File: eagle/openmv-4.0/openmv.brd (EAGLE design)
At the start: 25.4 x 33.3 mm, 42 parts, among them U1 OV9650, U2 USD-47571, U3 ADP322, U4 STM32F407LQFP100, U5 BEAD, X1 USB-MICROB, Y2 RESONATORSMD

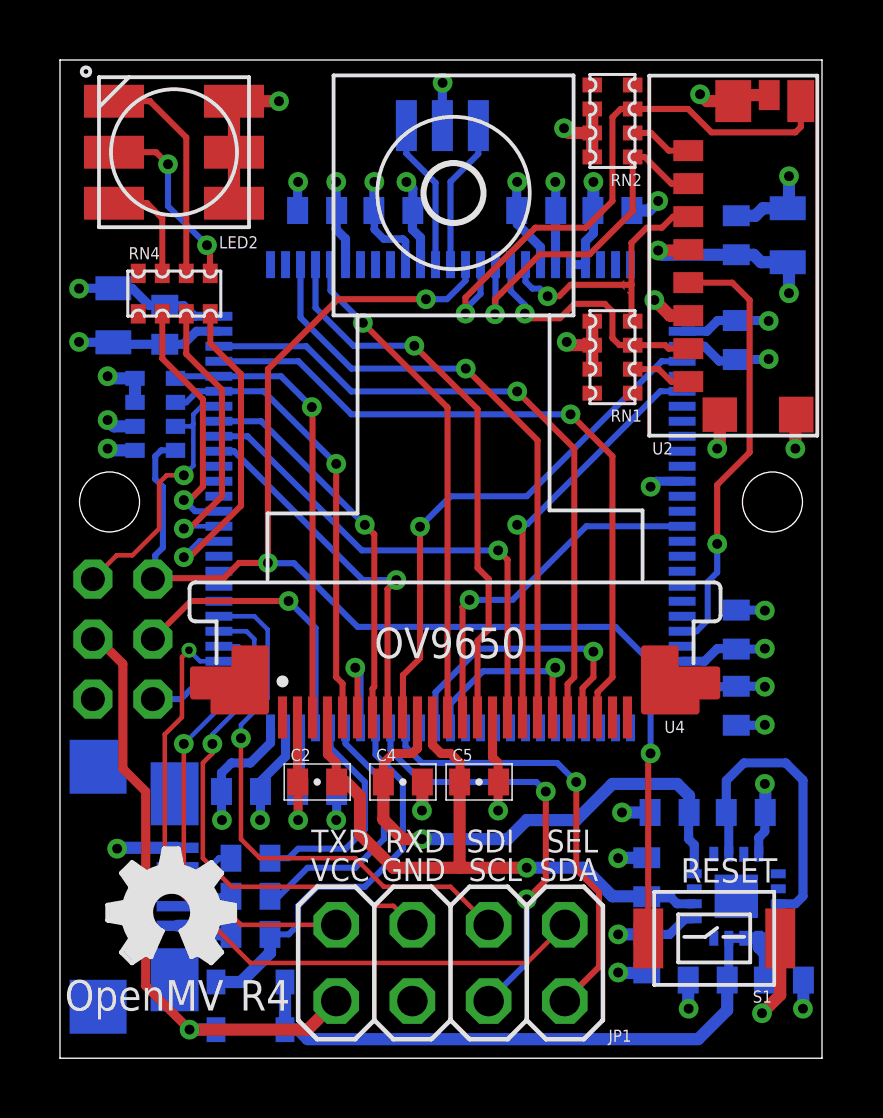
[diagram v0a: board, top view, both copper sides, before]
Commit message: Update REV4
* Add regulator test points
* Remove 10mil via
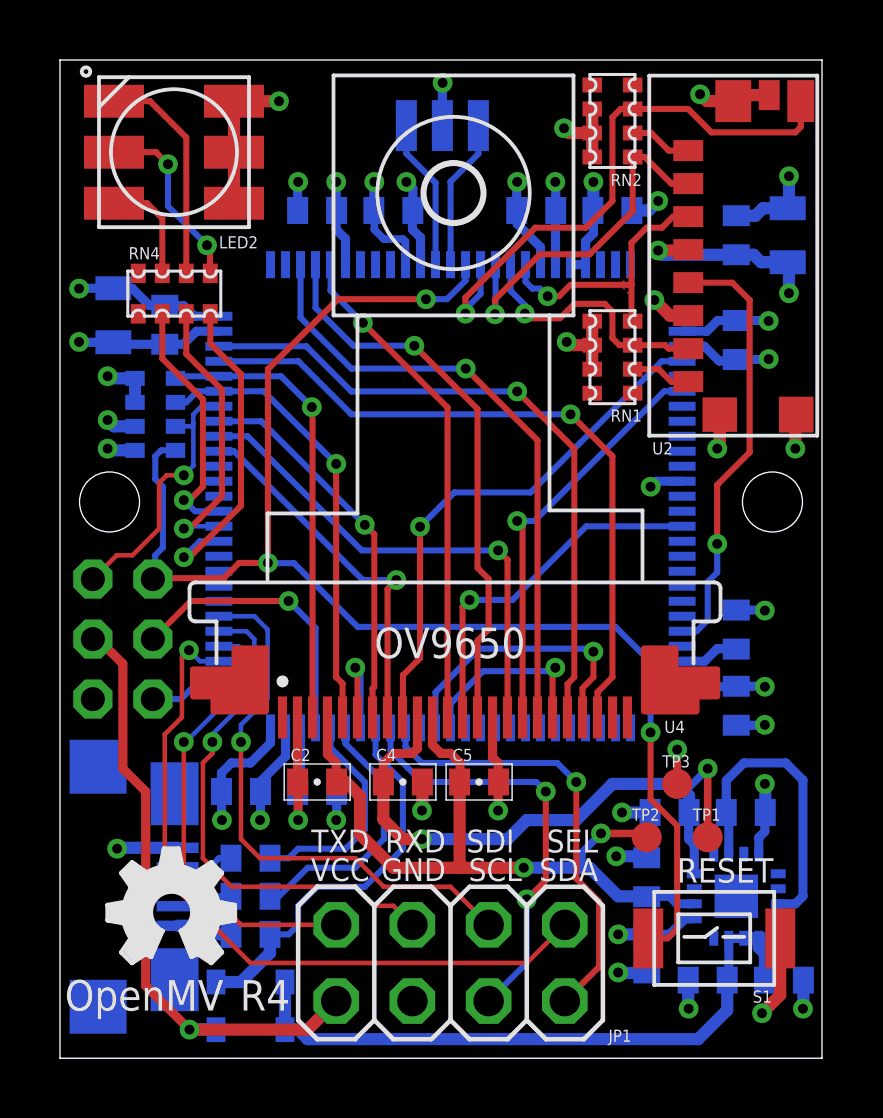
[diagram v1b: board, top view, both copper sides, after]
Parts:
- added TP1, TP2, TP3: TPTP10R, testpad:TP10R
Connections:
- net 1.8V: now also TP1.TP
- net 2.8V: now also TP2.TP
- net VCC: now also TP3.TP
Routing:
- net 1.8V: track 18.9 -> 22.3 mm, vias 1 -> 2
- net 2.8V: track 22.2 -> 25.2 mm, vias 1 -> 2
- net VCC: track 49.6 -> 50.7 mm, vias 16 -> 17
- net NRST: track 47.3 -> 48.4 mm
- net VCAP1: track 2.94 -> 1.99 mm, vias 1 -> 0

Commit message: Update REV4
* Use a different I2C multiplexed with USART
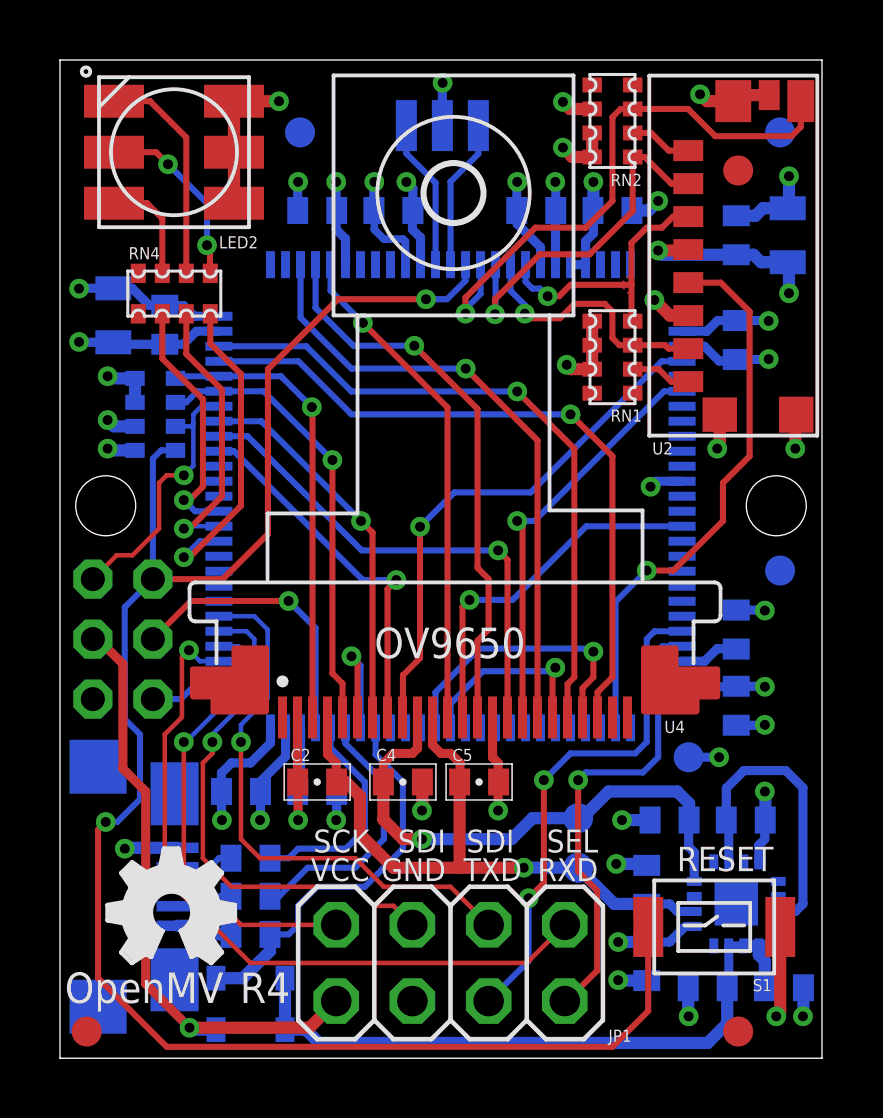
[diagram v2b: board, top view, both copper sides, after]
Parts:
- added JP3, JP4, JP5, JP6, JP7, JP8: FIDUCIAL1X2, sfe:FIDUCIAL-1X2
- moved TP1 4.36 mm to (17.3, 8.00), flipped to the bottom
- moved TP2 2.50 mm to (17.3, 6.35), flipped to the bottom
- moved TP3 0.97 mm to (21.0, 10.0), flipped to the bottom, turned to 180 degrees
- moved S1 0.38 mm to (21.8, 4.43)
- moved C15 0.25 mm to (24.1, 2.35)
- moved C16 0.25 mm to (21.6, 2.35)
- moved C20 0.25 mm to (19.6, 3.24)
- moved C17 0.25 mm to (22.9, 7.94)
- moved C18 0.25 mm to (20.3, 7.94)
- moved C19 0.25 mm to (19.6, 5.78)
- moved U3 0.25 mm to (22.5, 5.14)
- moved D1 0.13 mm to (6.35, 2.67)
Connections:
- removed net I2C3_SCL: JP1.4, U4.67
- new net I2C2_SCL: JP1.4, U4.47
- new net I2C2_SDA: JP1.2, U4.48
- net I2C3_SDA: no longer JP1.2
- net SD_SCLK: now also U4.52; no longer U4.47
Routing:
- net I2C2_SCL: track 0.00 -> 16.8 mm, vias 0 -> 2
- net I2C2_SDA: track 0.00 -> 15.5 mm, vias 0 -> 1
- net I2C3_SDA: track 14.9 -> 0.00 mm, vias 1 -> 0
- net I2C3_SCL: track 14.3 -> 0.00 mm, vias 2 -> 0
- net NRST: track 48.4 -> 60.5 mm, vias 3 -> 2
- net SD_SCLK: track 14.5 -> 18.7 mm
- net 1.8V: track 22.3 -> 18.8 mm, vias 2 -> 1
- net 2.8V: track 25.2 -> 22.3 mm, vias 2 -> 1
- net RESET: track 3.77 -> 4.63 mm
- net VCC: track 50.7 -> 51.0 mm, vias 17 -> 18
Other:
- board text added: "SCK"
- board text removed: "SCL"
- board text removed: "SDA"

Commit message: Update HW REV4
* Use dual LDO
* Add I2C EEPROM
* Update RESET switch
* Add bulk cap to STM VCC
* Add diode on debug VCC
* Add bead for sensor filter
* Use separate USART
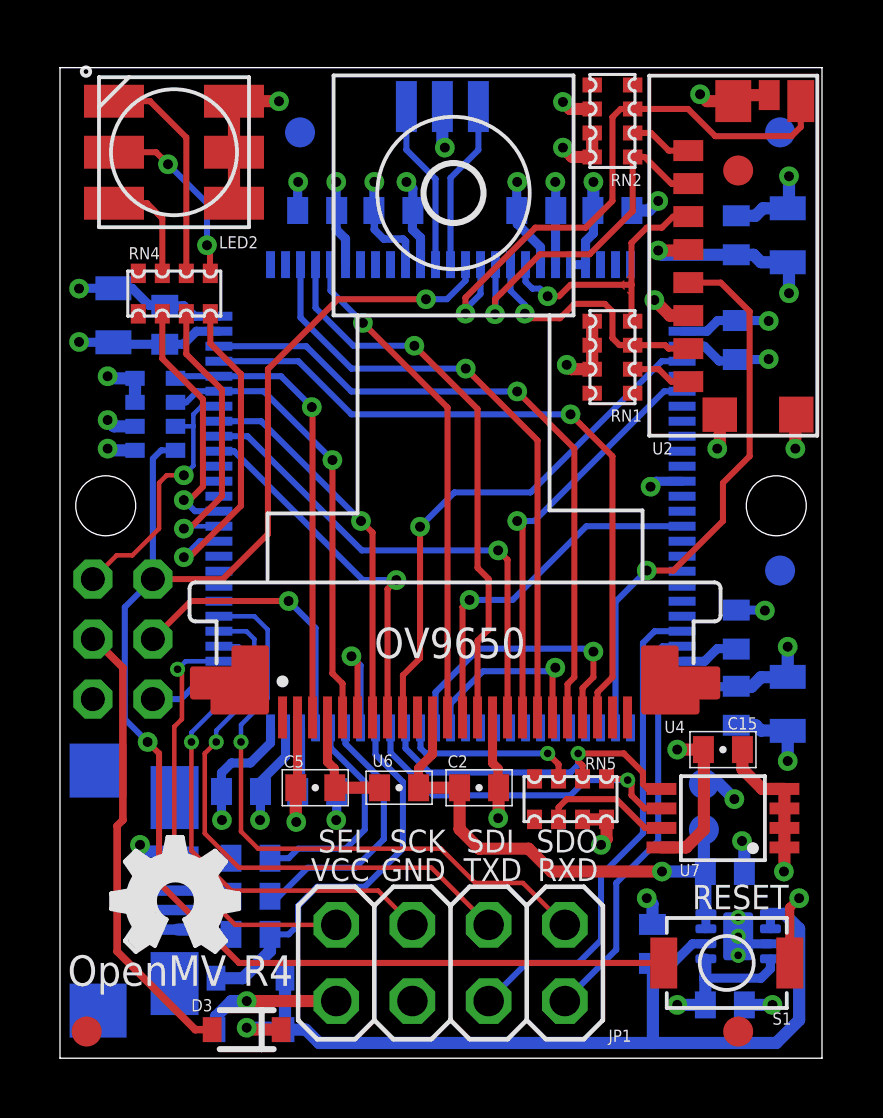
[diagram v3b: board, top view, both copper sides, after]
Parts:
- removed C17, C18: 1uF, sfe:0402-CAP
- removed TP3: TPTP10R, testpad:TP10R
- added D3: (no value), sfe:SOD-323
- added RN5: (no value), resistor-dil:CAT16
- added U6: BEAD, heka:0402-CAP
- added U7: 24FC128, mux:MSOP8
- C15: value 1uF -> 0.1uF
- C2, C5: value 0.1uF -> 4.7uF
- C24: value 10uF -> 22uF
- C25: value 10uF -> 47uF
- C4: value 0.1uF -> 22uF; device sfe:0402-CAP -> sfe:0805
- S1: value SWITCH -> SPST_3X4X2; device mux:1185S -> bt_electromech:3X4X2TACT
- U3: value ADP322 -> ADP222; device iofault:WFQFN-16 -> mux:LFCSP8
- moved C4 13.1 mm to (24.3, 11.8), flipped to the bottom, turned to 90 degrees
- moved C15 8.19 mm to (22.1, 10.3), flipped to the top, turned to 0 degrees
- moved C5 5.46 mm to (8.51, 9.02), turned to 180 degrees
- moved C2 5.40 mm to (14.0, 9.02), turned to 0 degrees
- moved TP2 4.38 mm to (21.5, 7.62), turned to 90 degrees
- moved TP1 4.34 mm to (21.5, 9.14), turned to 180 degrees
- moved C20 2.99 mm to (22.2, 1.78), turned to 180 degrees
- moved C19 2.64 mm to (22.2, 6.22), turned to 180 degrees
- moved C16 2.35 mm to (19.7, 3.81), turned to 90 degrees
- moved S1 1.32 mm to (22.2, 3.17), turned to 180 degrees
- moved U3 1.08 mm to (22.6, 4.06), turned to 0 degrees
- moved Y2 0.64 mm to (12.7, 31.7)
- moved LOGO1 0.40 mm to (1.71, 3.56)
- moved X1 0.13 mm to (1.27, 5.59)
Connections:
- removed net 1.8V: C18.1, C4.1, TP1.TP, U1.P$10, U3.8
- removed net I2C3_SDA: U4.66
- new net EEP_SCL: RN5.1, U4.67, U7.6
- new net EEP_SDA: RN5.2, U4.66, U7.5
- new net EEP_WP: RN5.3, U4.65
- new net N$10: C5.1, U1.P$4, U6.1
- new net N$11: D3.2, JP2.4
- new net N$9: RN5.6, U7.7
- net 2.8V: now also U3.7, U3.8, U6.2; no longer C5.1, U1.P$4, U3.6
- net GND: now also C4.1, S1.P$1, U3.3, U3.EXP, U7.1, U7.2, U7.3, U7.4; no longer C17.2, C18.2, C4.2, S1.P$2, U3.12
- net NRST: now also S1.P$2; no longer S1.P$1
- net RAW: no longer JP2.4
- net SPI3_MISO: now also JP1.3; no longer JP1.5
- net SPI3_MOSI: now also JP1.1; no longer JP1.3
- net SPI3_SCLK: now also JP1.5; no longer JP1.7
- net SPI3_SSEL: now also JP1.7; no longer JP1.1
- net VCC: now also C15.1, C4.2, RN5.7, RN5.8, TP1.TP, U3.4, U7.8; no longer TP3.TP
- net VIN: now also D3.1, U3.6; no longer C15.1, C17.1, U3.10, U3.15, U3.16, U3.3
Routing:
- net 1.8V: track 18.8 -> 0.00 mm, vias 1 -> 0
- net RAW: track 20.6 -> 4.66 mm
- net N$11: track 0.00 -> 15.2 mm
- net EEP_SCL: track 0.00 -> 12.0 mm, vias 0 -> 1
- net EEP_SDA: track 0.00 -> 11.7 mm, vias 0 -> 1
- net VCC: track 51.0 -> 62.4 mm, vias 18 -> 20
- net SPI3_SSEL: track 24.4 -> 14.4 mm
- net NRST: track 60.5 -> 52.1 mm
- net EEP_WP: track 0.00 -> 5.99 mm, vias 0 -> 1
- net 2.8V: track 22.3 -> 17.4 mm
- net N$9: track 0.00 -> 4.34 mm
- net N$10: track 0.00 -> 3.94 mm
- net VIN: track 34.0 -> 31.3 mm, vias 0 -> 1
- net SPI3_MOSI: track 18.6 -> 21.0 mm
- net SPI3_MISO: track 17.2 -> 19.2 mm
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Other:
- board size 25.4 x 33.3 mm -> 25.4 x 33 mm
- board text added: "SDO"

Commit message: Update REV4
* Make more room for mounting holes, and dbg header
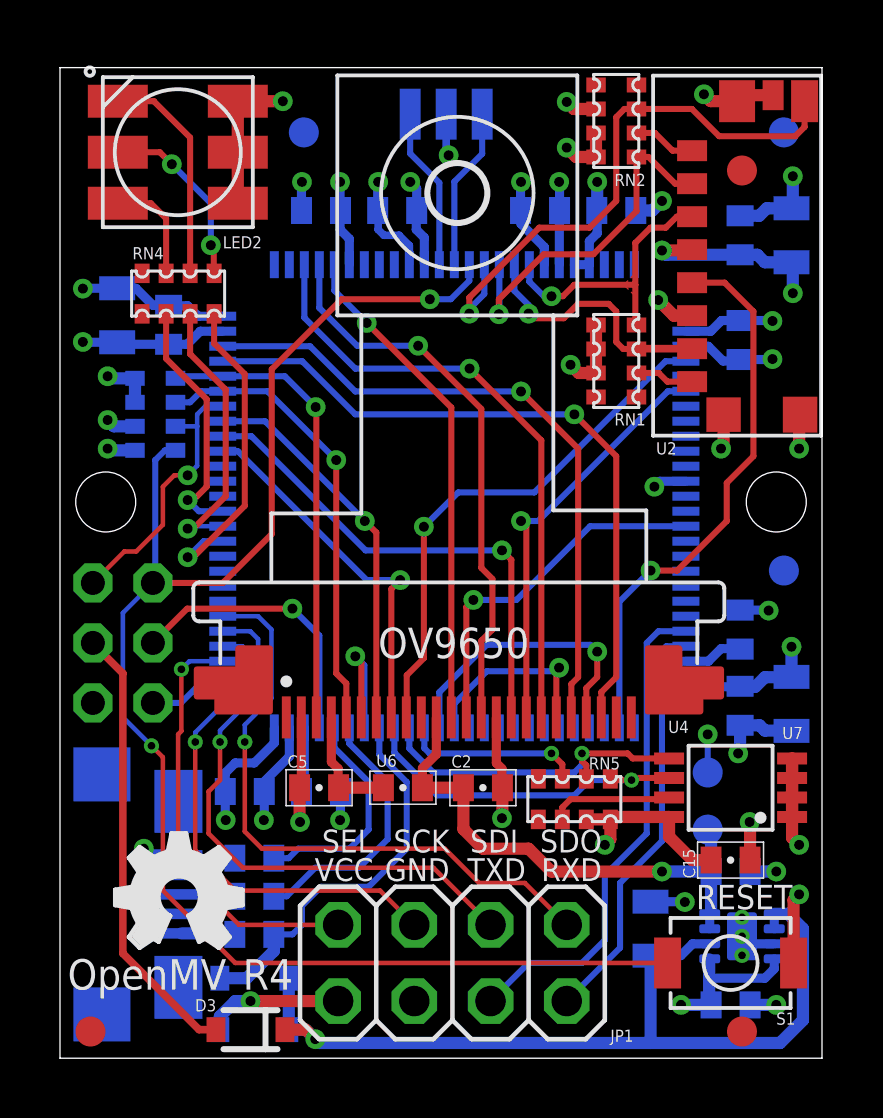
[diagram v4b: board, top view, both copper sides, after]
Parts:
- C16: value 1uF -> 10uF; device sfe:0402-CAP -> sfe:0805
- moved C15 3.69 mm to (22.4, 6.60)
- moved U7 1.05 mm to (22.4, 9.02)
- moved C16 0.51 mm to (19.7, 4.32)
- moved TP1 0.40 mm to (21.6, 9.53)
- moved Y2 0.28 mm to (12.9, 31.5)
- moved C19 0.19 mm to (22.4, 6.22)
- moved C20 0.19 mm to (22.4, 1.78)
- moved RN1 0.18 mm to (18.5, 23.2)
- moved LOGO1 0.18 mm to (1.84, 3.68)
- moved X1 0.18 mm to (1.40, 5.46)
- moved C14 0.13 mm to (18.5, 28.3)
- moved RN2 0.13 mm to (18.5, 31.2)
- moved C10 0.13 mm to (6.16, 8.89)
- moved C12 0.13 mm to (8.70, 8.89)
- moved C9 0.13 mm to (8.70, 28.3)
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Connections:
- new net N$12: U4.53
- new net N$13: U4.54
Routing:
- net GND: track 56.8 -> 57.8 mm, vias 29 -> 30
- net VIN: track 31.3 -> 30.3 mm
- net VCC: track 62.4 -> 61.7 mm, vias 20 -> 19
- net EEP_SDA: track 11.7 -> 11.1 mm

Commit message: Update REV4
* Replace regulator with ADP121xx
* Use the new crystal
* Fix USB connector
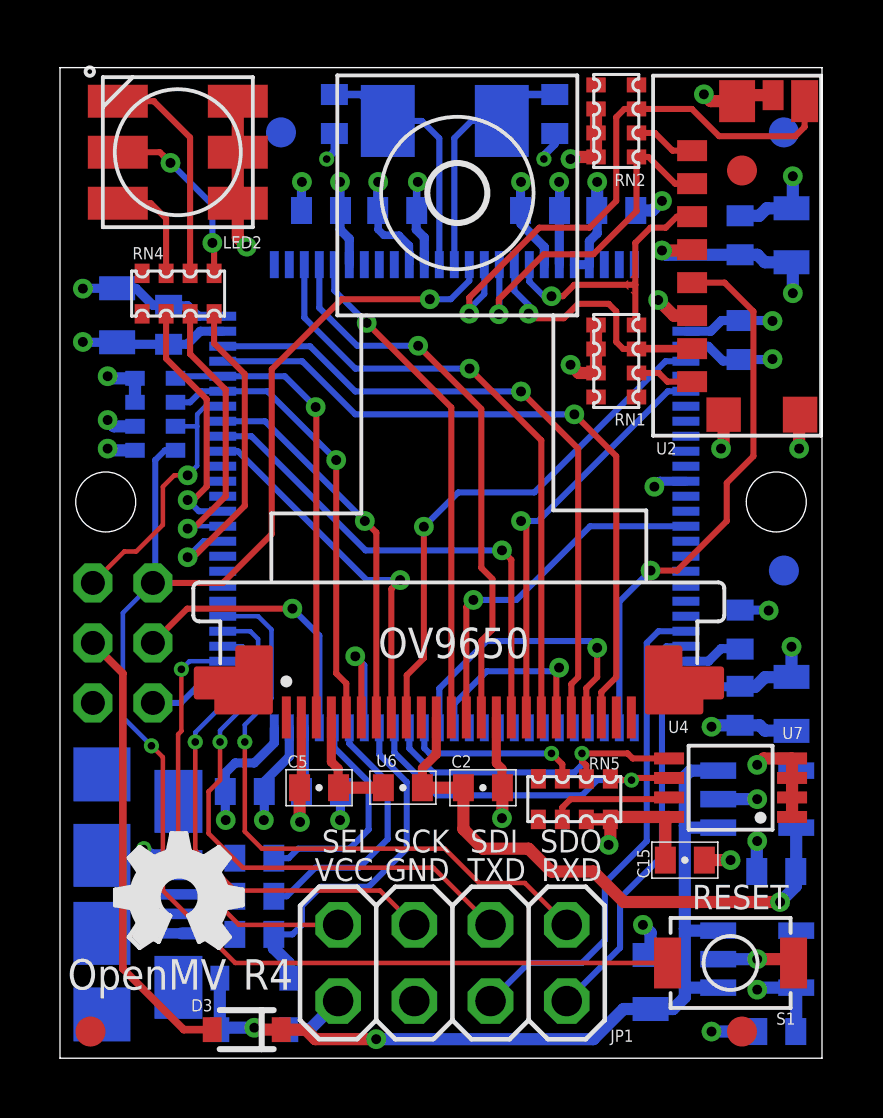
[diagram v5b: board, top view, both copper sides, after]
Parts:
- removed TP1, TP2: TPTP10R, testpad:TP10R
- removed Y2: RESONATORSMD, sfe:RESONATOR-SMD
- added C17, C18: 18pF, sfe:0402-CAP
- added U8: VREG_25, sfe:SOT23-5
- added X2: (no value), adafruit:NX5032
- U3: value ADP222 -> VREG_33; device mux:LFCSP8 -> sfe:SOT23-5
- moved C16 1.78 mm to (19.7, 2.54)
- moved C20 1.76 mm to (23.9, 0.89), turned to 0 degrees
- moved C15 1.52 mm to (20.8, 6.60)
- moved C19 1.52 mm to (23.9, 6.22), turned to 0 degrees
- moved U3 0.92 mm to (23.2, 3.30), turned to 90 degrees
- moved JP8 0.76 mm to (7.37, 30.9)
- moved D3 0.13 mm to (6.22, 0.95)
- turned D1 to 180 degrees
- turned D2 to 180 degrees
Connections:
- net 2.8V: now also U8.5; no longer TP2.TP, U3.7, U3.8
- net GND: now also C17.1, C18.1, U3.2, U8.2; no longer U3.3, U3.EXP, Y2.2
- net N$6: now also C17.2, X2.P$1; no longer Y2.1
- net N$8: now also C18.2, X2.P$2; no longer Y2.3
- net VCC: no longer TP1.TP, U3.4
- net VIN: now also U3.3, U8.1, U8.3; no longer U3.2, U3.6
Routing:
- net VCC: track 61.7 -> 56.6 mm, vias 19 -> 17
- net N$6: track 5.40 -> 8.67 mm
- net N$8: track 5.42 -> 8.31 mm
- net RAW: track 4.59 -> 2.04 mm, vias 1 -> 0
- net 2.8V: track 17.5 -> 19.5 mm
- net VBUS: track 13.1 -> 12.1 mm
- net GND: track 57.8 -> 57.3 mm, vias 30 -> 29
- net VIN: track 30.3 -> 29.9 mm, vias 1 -> 2
